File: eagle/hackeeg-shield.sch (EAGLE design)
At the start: 140 parts, among them IC1 ADS1299IPAG, IC10 TXB0108PWR, IC11 TXB0108PWR, IC2 TPS72325DBVT, IC3 TPS73225DBVT, IC5 24AA256UID, IC6 TPS60403DBVT, IC7 OPA376DBV, IC8 OPA376DBV, IC9 TXS0102DCUR

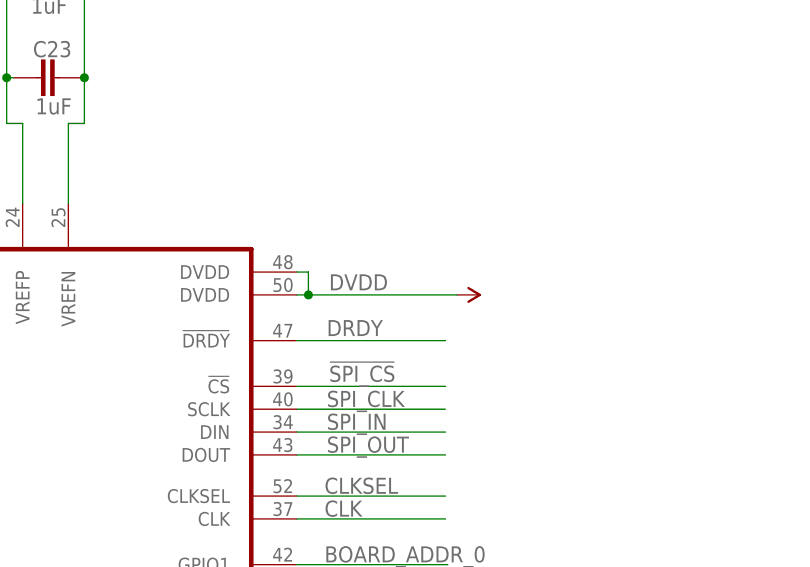
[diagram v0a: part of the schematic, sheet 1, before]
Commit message: changed inner layer (AGND and DVDD) polygon isolate clearance to 12 mils (from 0)
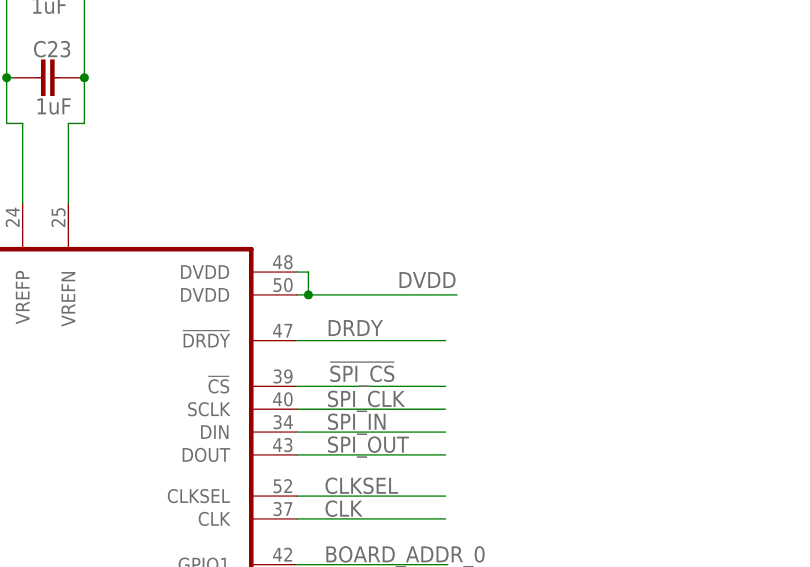
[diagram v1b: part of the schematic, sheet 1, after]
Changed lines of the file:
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@@
 <part name="SUPPLY13" library="supply2" deviceset="AGND" device=""/>
 <part name="SUPPLY22" library="SparkFun-Aesthetics" deviceset="3.3V" device="" value="AVDD"/>
-<part name="SUPPLY24" library="SparkFun-Aesthetics" deviceset="3.3V" device="" value="DVDD"/>
 <part name="AVSS3" library="SparkFun-Aesthetics" deviceset="GND" device="" value="AVSS"/>
 <part name="C31" library="SparkFun-Passives" deviceset="CAP" device="0603-CAP" value="0.01uF"/>
@@
 <instance part="SUPPLY13" gate="G$1" x="218.186" y="107.696"/>
 <instance part="SUPPLY22" gate="G$1" x="276.098" y="236.982"/>
-<instance part="SUPPLY24" gate="G$1" x="344.678" y="215.392" smashed="yes" rot="R270">
-<attribute name="VALUE" x="330.454" y="215.9" size="1.778" layer="96"/>
-</instance>
 <instance part="AVSS3" gate="1" x="236.22" y="106.68" smashed="yes">
 <attribute name="VALUE" x="233.68" y="104.14" size="1.778" layer="96"/>
@@
 <pinref part="IC1" gate="G$1" pin="DVDD@1"/>
 <pinref part="IC1" gate="G$1" pin="DVDD@2"/>
-<pinref part="SUPPLY24" gate="G$1" pin="3.3V"/>
-</segment>
-<segment>
+<label x="338.074" y="216.154" size="1.778" layer="95"/>
+</segment>
+<segment>

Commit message: updated board version number to 1.2.4
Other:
- note added: "v1.2.4"
- note removed: "v1.1"
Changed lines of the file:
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@@
 By-Attribution Share-Alike 4.0 license</text>
 <text x="328.676" y="37.592" size="2.54" layer="95">Copyright 2013 Adam Feuer</text>
-<text x="416.306" y="7.112" size="2.1844" layer="95">v1.1</text>
+<text x="416.306" y="7.112" size="2.1844" layer="95">v1.2.4</text>
 <text x="246.634" y="212.344" size="1.778" layer="91">NC</text>
 <text x="327.406" y="161.798" size="1.27" layer="91">NC</text>

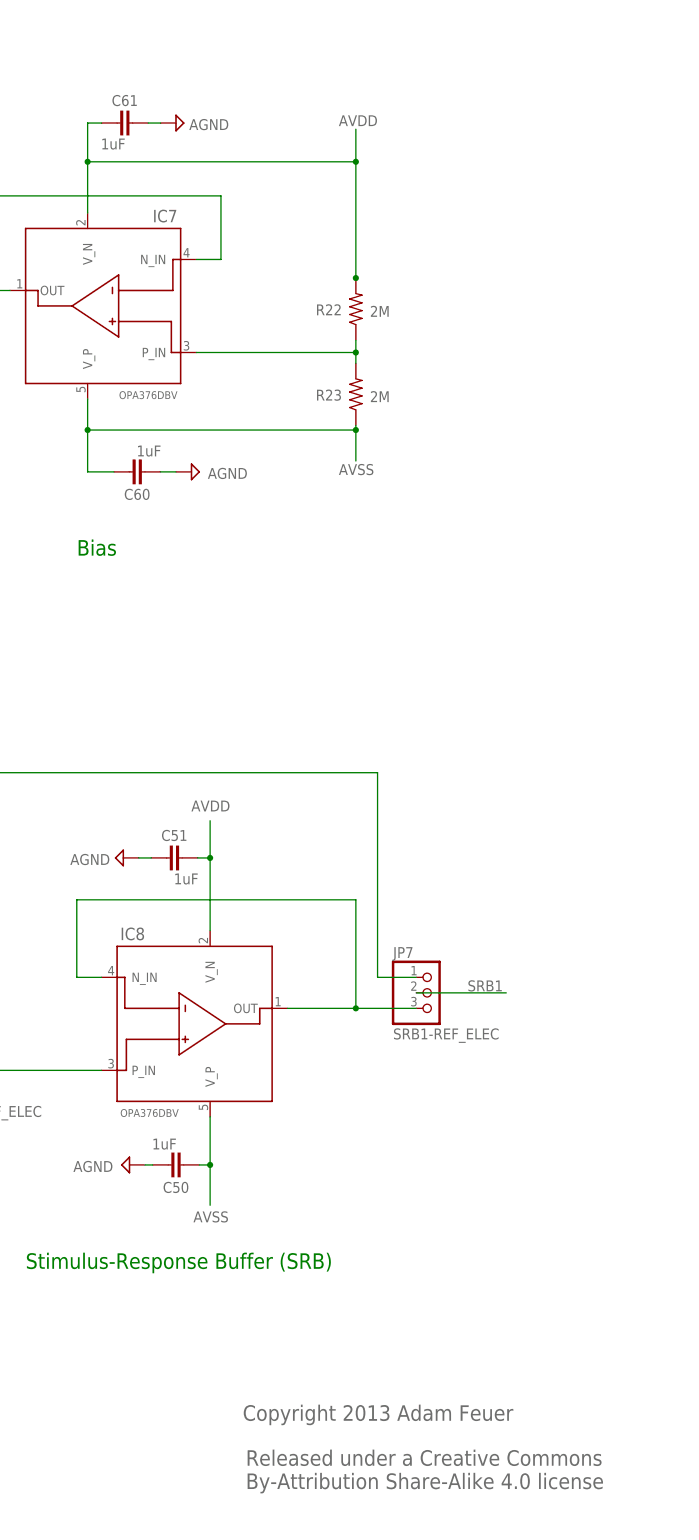
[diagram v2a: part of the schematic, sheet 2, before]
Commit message: fixed schematic and board bug - opamp OPA376 VDD and VSS pins were reversed; updated schematic and board version to 1.3.1
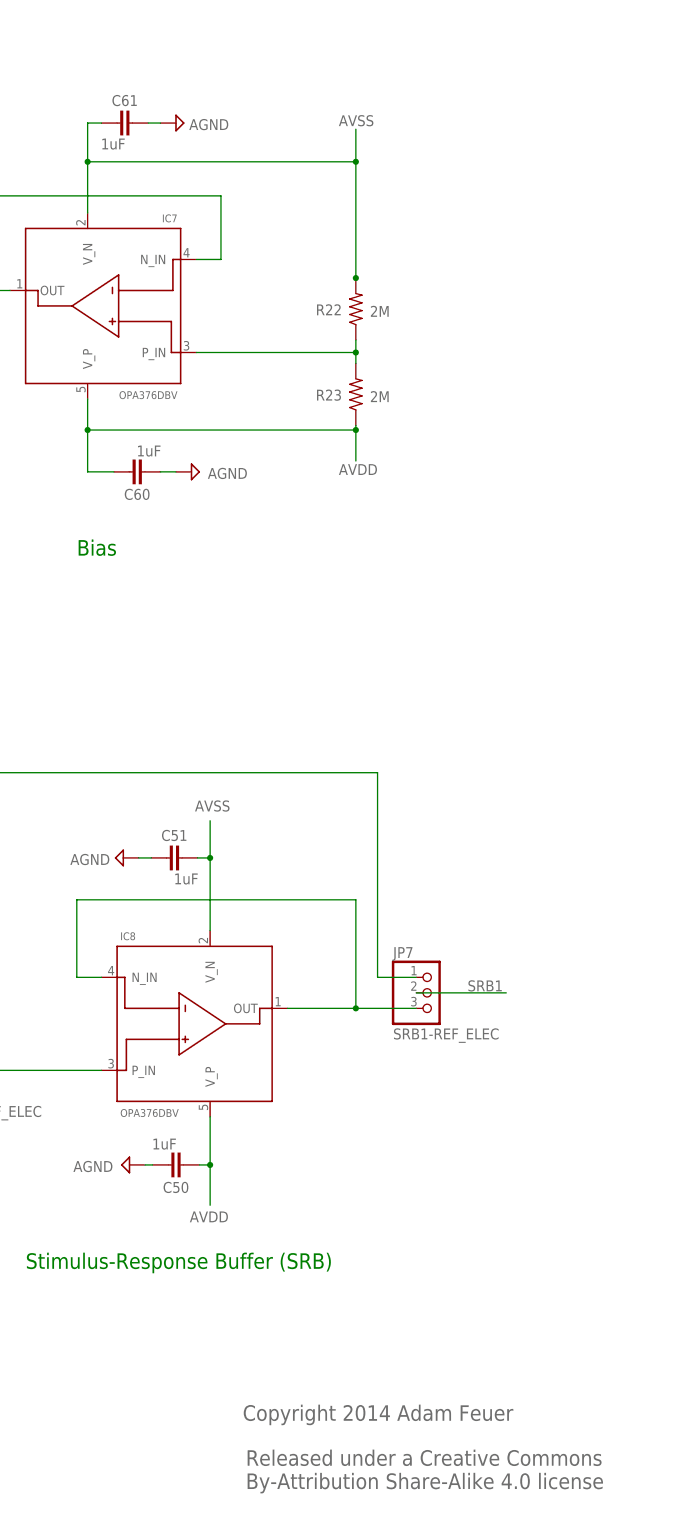
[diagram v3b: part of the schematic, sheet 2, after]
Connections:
- net AVDD: now also C50.1, C60.1, IC7.V_P, IC8.V_P, R23.1; no longer C51.2, C61.2, IC7.V_N, IC8.V_N, R22.2
- net AVSS: now also C51.2, C61.2, IC7.V_N, IC8.V_N, R22.2; no longer C50.1, C60.1, IC7.V_P, IC8.V_P, R23.1
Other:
- note added: "Copyright 2014 Adam Feuer"
- note added: "v1.3.1"
- note removed: "Copyright 2013 Adam Feuer"
- note removed: "v1.2.4"

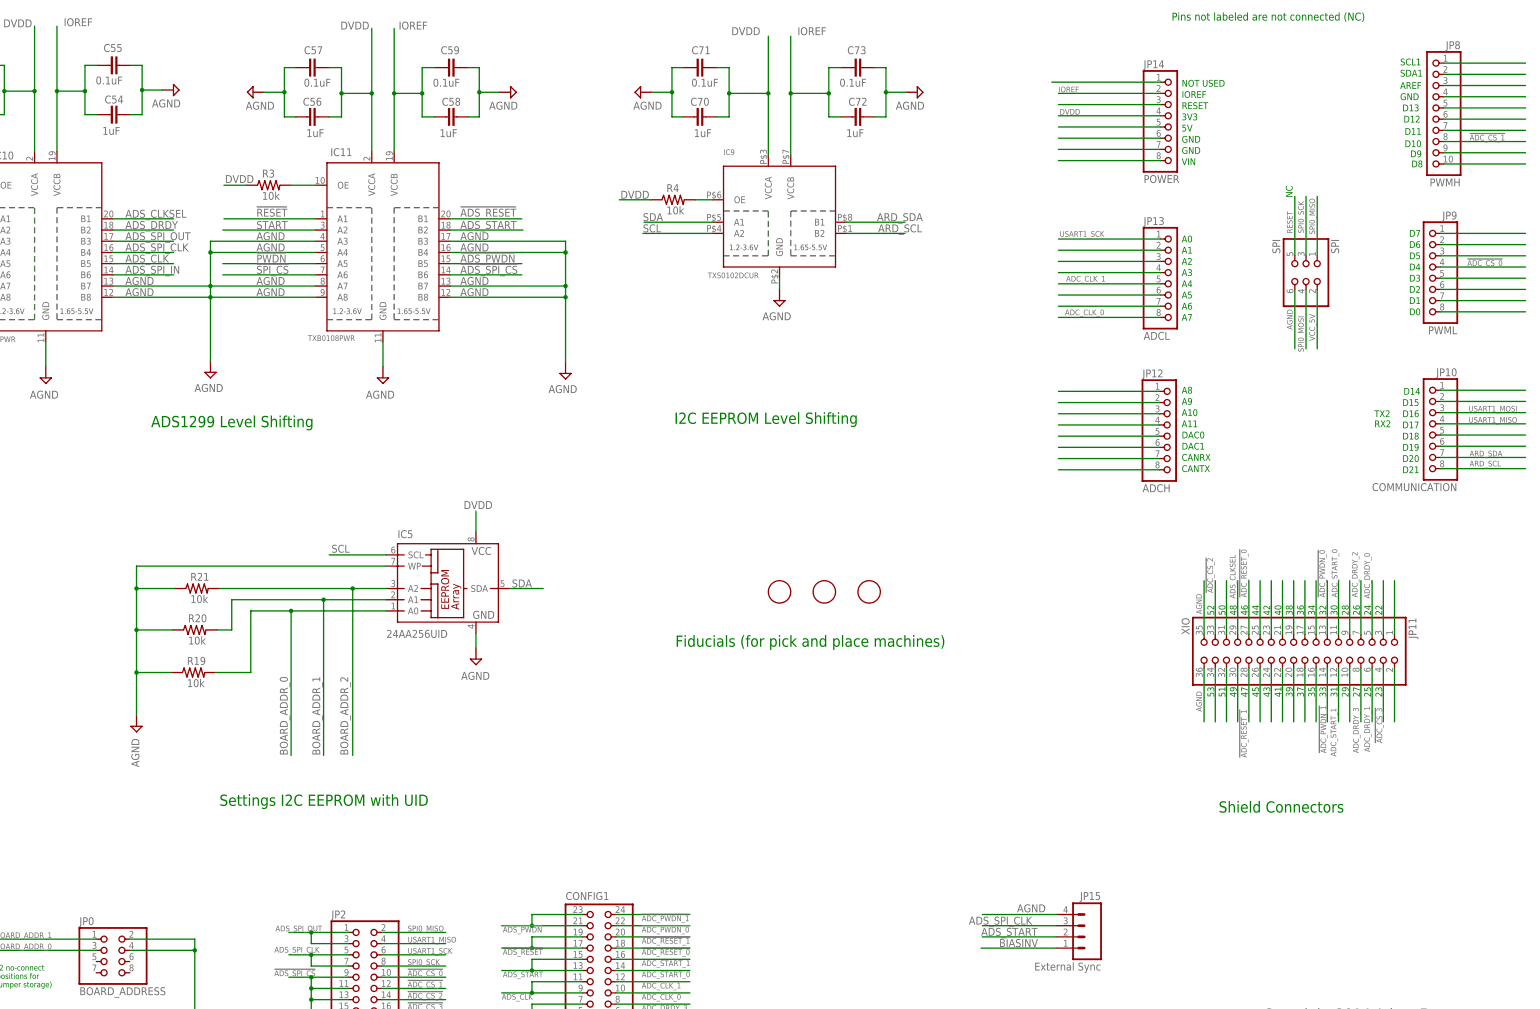
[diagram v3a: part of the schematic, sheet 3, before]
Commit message: improved AVSS trace width on bottom layer; removed trace running through the middle of caps; improved text sizes for configuration labels
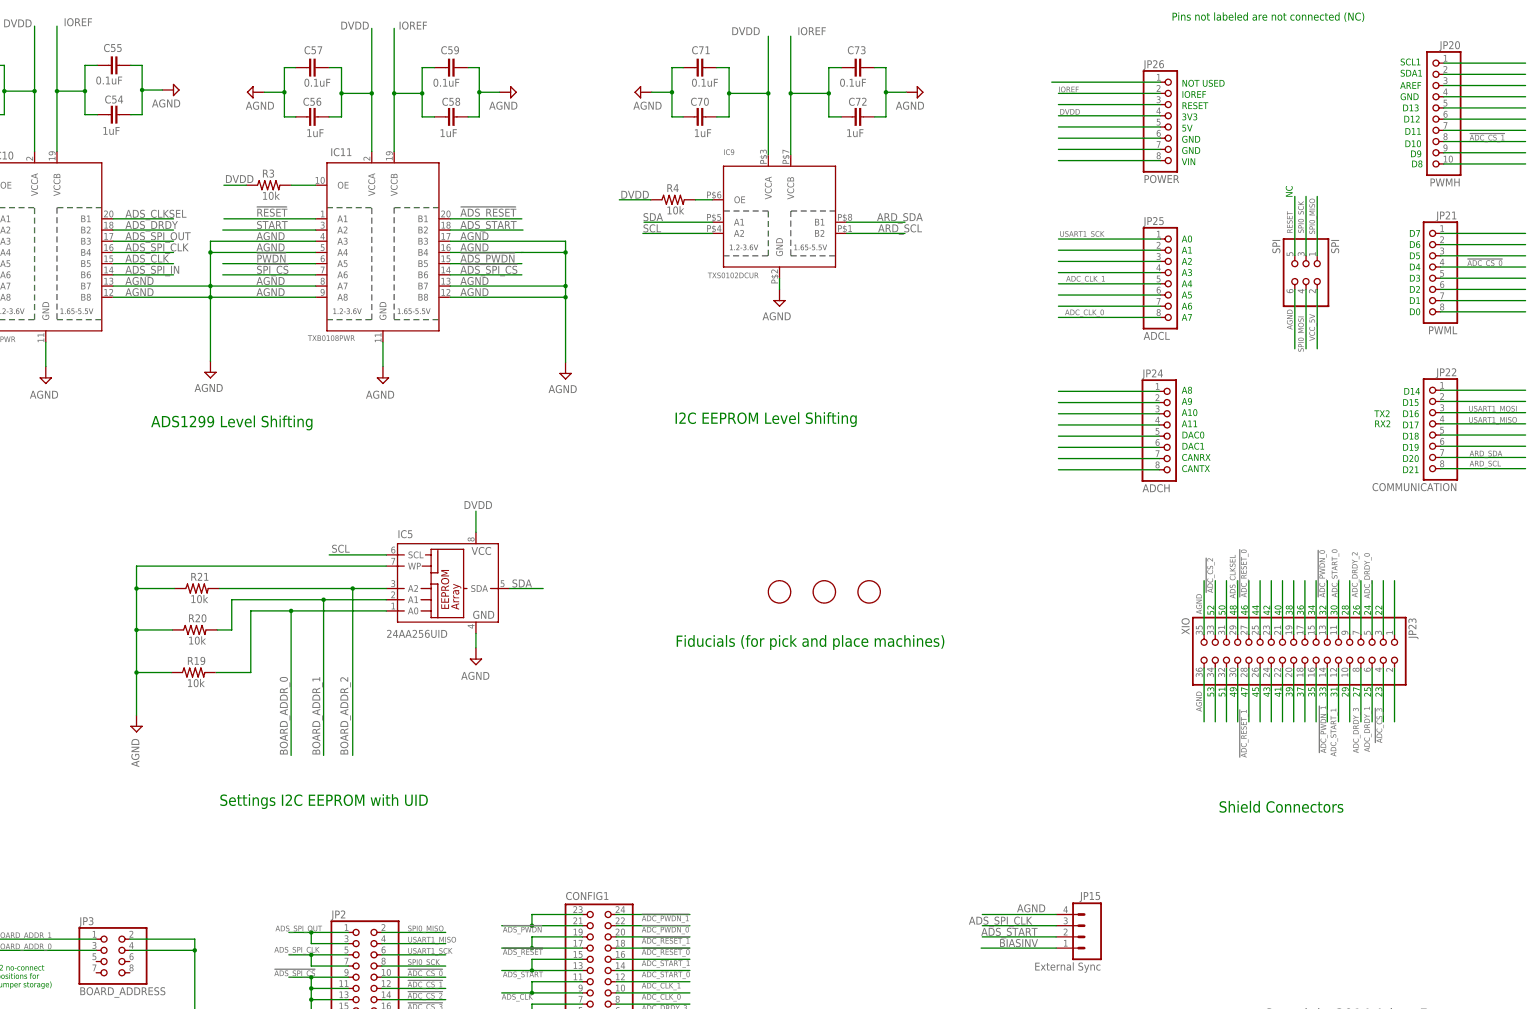
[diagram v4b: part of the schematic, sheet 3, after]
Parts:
- removed JP0: BOARD_ADDRESS, headers:PINHD-2X4
- added JP20: PWMH, SmartPrj:PINHD-1X10
- JP3: value 5V-2.5V -> BOARD_ADDRESS; device headers:PINHD-1X3 -> headers:PINHD-2X4
- JP4: value -2.5V-GND -> 5V-2.5V
- JP5: value SRB1-BIAS -> -2.5V-GND; device adafruit:PINHD-1X3 -> headers:PINHD-1X3
- JP6: value SRB2-REF_ELEC -> SRB1-BIAS
- JP7: value SRB1-REF_ELEC -> SRB2-REF_ELEC
- JP8: value PWMH -> SRB1-REF_ELEC; device SmartPrj:PINHD-1X10 -> adafruit:PINHD-1X3
- renumbered JP10 to JP22, JP11 to JP23, JP12 to JP24, JP13 to JP25, JP14 to JP26, JP9 to JP21
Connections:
- net !ADC_CS_1: now also JP20.8; no longer JP8.8
- net +2.5V: now also JP4.3; no longer JP3.3
- net -2.5V: now also JP5.1; no longer JP4.1
- net AGND: now also JP5.3; no longer JP4.3
- net AVDD: now also JP4.2; no longer JP3.2
- net AVSS: now also JP5.2; no longer JP4.2
- net BIAS_ELEC: now also JP6.1; no longer JP5.1
- net BOARD_ADDR_0: now also JP3.3; no longer JP0.3
- net BOARD_ADDR_1: now also JP3.1; no longer JP0.1
- net DVDD: now also JP3.2, JP3.4; no longer JP0.2, JP0.4
- net N$16: now also JP7.2; no longer JP6.2
- net N$17: now also JP8.3; no longer JP7.3
- net N$18: now also JP6.3; no longer JP5.3
- net N$27: now also JP20.3; no longer JP8.3
- net N$28: now also JP20.4; no longer JP8.4
- net N$29: now also JP20.5; no longer JP8.5
- net N$30: now also JP20.6; no longer JP8.6
- net N$31: now also JP20.7; no longer JP8.7
- net N$33: now also JP20.10; no longer JP8.10
- net N$6: now also JP20.9; no longer JP8.9
- net N$6001: now also JP20.2; no longer JP8.2
- net N$6002: now also JP20.1; no longer JP8.1
- net REF_ELEC: now also JP8.1; no longer JP6.1
- net SRB1: now also JP6.2, JP8.2; no longer JP5.2, JP7.2
- net SRB2: now also JP7.3; no longer JP6.3
- net VCC_5V_FILTERED: now also JP4.1; no longer JP3.1
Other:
- moved on the sheet: JP4, JP6, JP7
